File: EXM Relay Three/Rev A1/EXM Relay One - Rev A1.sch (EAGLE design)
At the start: 23 parts, among them J1 MSTBA3, J10 MSTBA2, J2 MSTBA3, J3 22-05-7038-03, J4 22-05-7038-03, J5 22-05-7038-03, J6 22-05-7038-03, J7 MSTBA3, J8 22-05-7038-03, J9 22-05-7038-03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

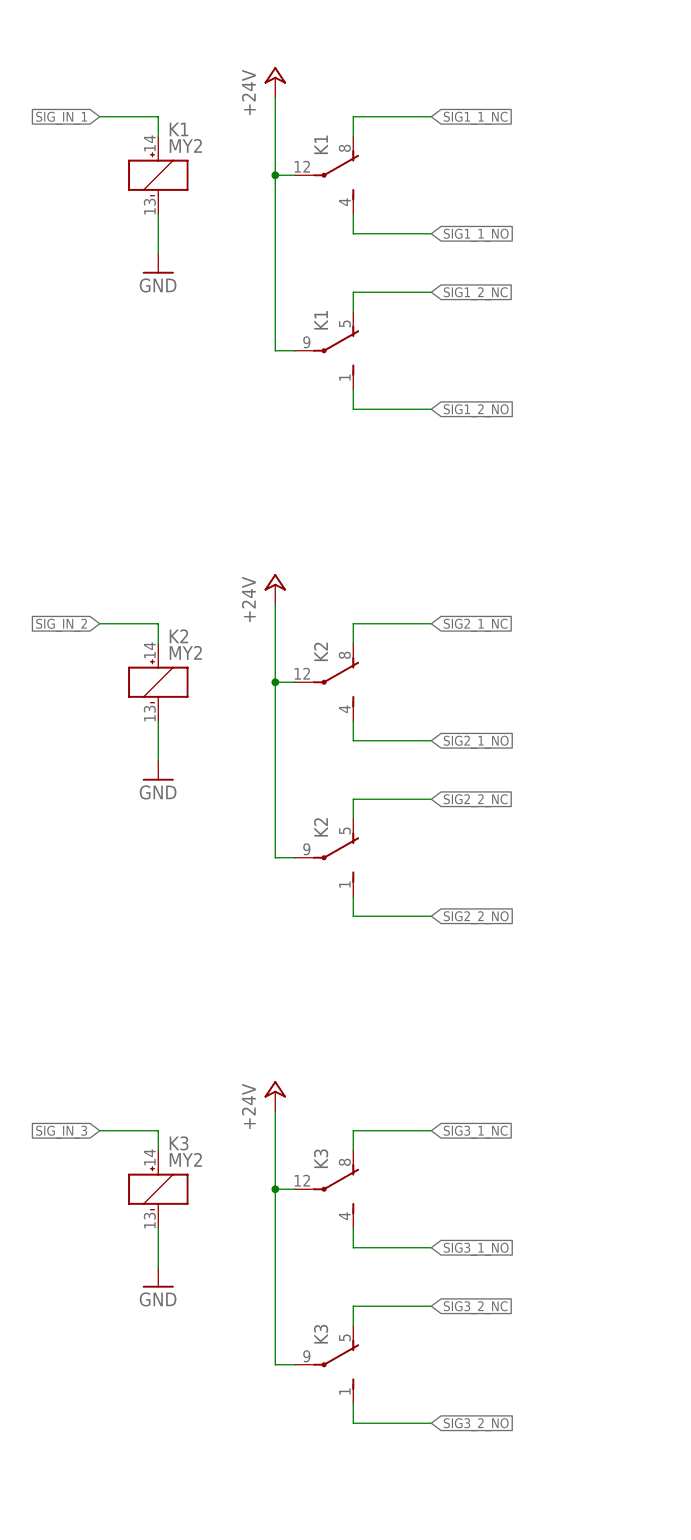
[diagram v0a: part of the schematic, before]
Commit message: Update relay device and re-route the board
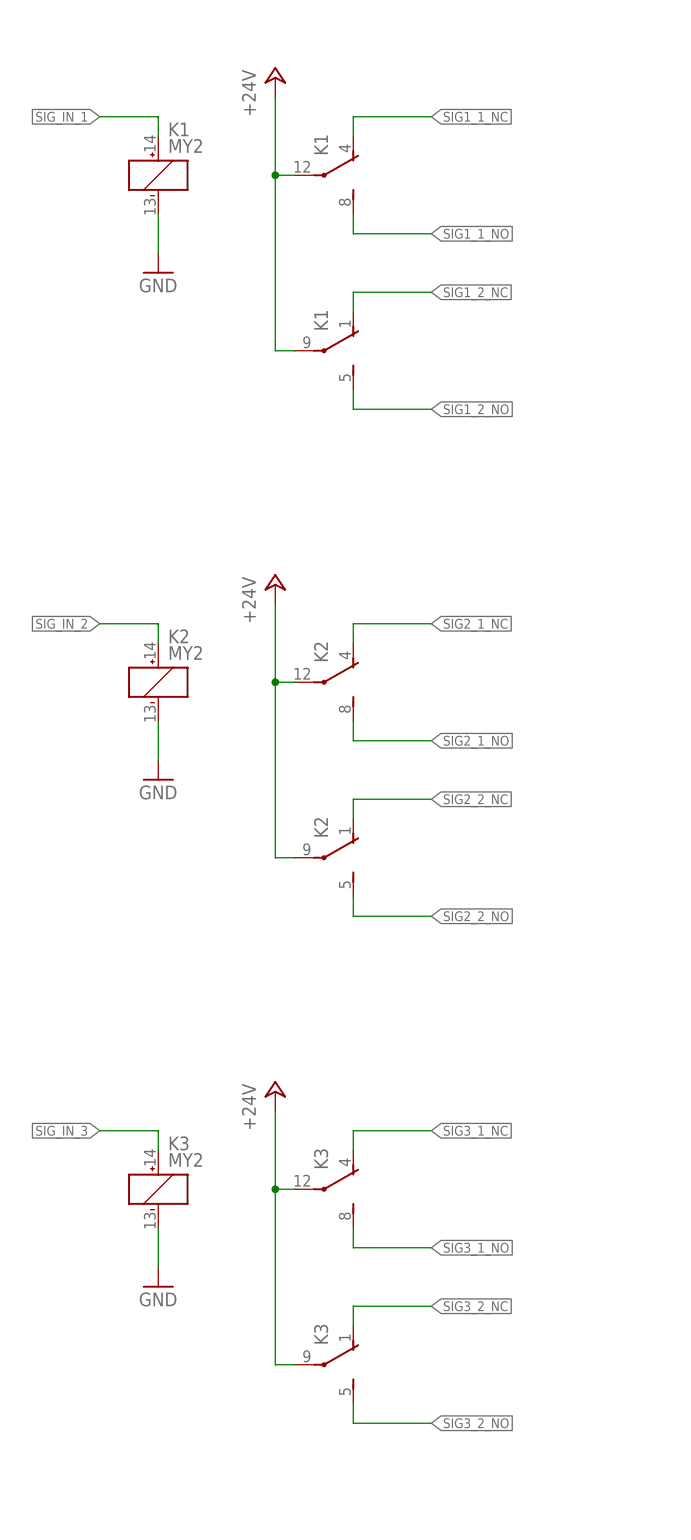
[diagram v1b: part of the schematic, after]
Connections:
- net SIG1_1_NC: now also K1G$2.NC; no longer K1G$2.NO
- net SIG1_1_NO: now also K1G$2.NO; no longer K1G$2.NC
- net SIG1_2_NC: now also K1G$3.NC; no longer K1G$3.NO
- net SIG1_2_NO: now also K1G$3.NO; no longer K1G$3.NC
- net SIG2_1_NC: now also K2G$2.NC; no longer K2G$2.NO
- net SIG2_1_NO: now also K2G$2.NO; no longer K2G$2.NC
- net SIG2_2_NC: now also K2G$3.NC; no longer K2G$3.NO
- net SIG2_2_NO: now also K2G$3.NO; no longer K2G$3.NC
- net SIG3_1_NC: now also K3G$2.NC; no longer K3G$2.NO
- net SIG3_1_NO: now also K3G$2.NO; no longer K3G$2.NC
- net SIG3_2_NC: now also K3G$3.NC; no longer K3G$3.NO
- net SIG3_2_NO: now also K3G$3.NO; no longer K3G$3.NC
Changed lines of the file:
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@@
 <segment>
 <wire x1="167.64" y1="144.78" x2="177.8" y2="144.78" width="0.1524" layer="91"/>
-<pinref part="K2" gate="G$2" pin="NC"/>
-<wire x1="167.64" y1="144.78" x2="167.64" y2="147.32" width="0.1524" layer="91"/>
 <label x="177.8" y="144.78" size="1.27" layer="95" xref="yes"/>
+<pinref part="K2" gate="G$2" pin="NO"/>
+<wire x1="167.64" y1="147.32" x2="167.64" y2="144.78" width="0.1524" layer="91"/>
 </segment>
 </net>
@@
 </segment>
 <segment>
-<pinref part="K1" gate="G$2" pin="NO"/>
-<wire x1="167.64" y1="223.52" x2="167.64" y2="226.06" width="0.1524" layer="91"/>
 <label x="177.8" y="226.06" size="1.27" layer="95" xref="yes"/>
 <wire x1="167.64" y1="226.06" x2="177.8" y2="226.06" width="0.1524" layer="91"/>
+<pinref part="K1" gate="G$2" pin="NC"/>
+<wire x1="167.64" y1="223.52" x2="167.64" y2="226.06" width="0.1524" layer="91"/>
 </segment>
 </net>
 <net name="SIG2_2_NC" class="0">
 <segment>
-<pinref part="K2" gate="G$3" pin="NO"/>
-<wire x1="167.64" y1="134.62" x2="167.64" y2="137.16" width="0.1524" layer="91"/>
 <wire x1="167.64" y1="137.16" x2="177.8" y2="137.16" width="0.1524" layer="91"/>
 <label x="177.8" y="137.16" size="1.27" layer="95" xref="yes"/>
+<pinref part="K2" gate="G$3" pin="NC"/>
+<wire x1="167.64" y1="137.16" x2="167.64" y2="134.62" width="0.1524" layer="91"/>
 </segment>
 <segment>
@@
 <net name="SIG2_2_NO" class="0">
 <segment>
-<pinref part="K2" gate="G$3" pin="NC"/>
-<wire x1="167.64" y1="124.46" x2="167.64" y2="121.92" width="0.1524" layer="91"/>
 <wire x1="167.64" y1="121.92" x2="177.8" y2="121.92" width="0.1524" layer="91"/>
 <label x="177.8" y="121.92" size="1.27" layer="95" xref="yes"/>
+<pinref part="K2" gate="G$3" pin="NO"/>
+<wire x1="167.64" y1="124.46" x2="167.64" y2="121.92" width="0.1524" layer="91"/>
 </segment>
 <segment>
@@
 </segment>
 <segment>
-<pinref part="K2" gate="G$2" pin="NO"/>
-<wire x1="167.64" y1="157.48" x2="167.64" y2="160.02" width="0.1524" layer="91"/>
 <label x="177.8" y="160.02" size="1.27" layer="95" xref="yes"/>
 <wire x1="167.64" y1="160.02" x2="177.8" y2="160.02" width="0.1524" layer="91"/>
+<pinref part="K2" gate="G$2" pin="NC"/>
+<wire x1="167.64" y1="157.48" x2="167.64" y2="160.02" width="0.1524" layer="91"/>
 </segment>
 </net>
@@
 <segment>
 <wire x1="167.64" y1="210.82" x2="177.8" y2="210.82" width="0.1524" layer="91"/>
-<pinref part="K1" gate="G$2" pin="NC"/>
-<wire x1="167.64" y1="210.82" x2="167.64" y2="213.36" width="0.1524" layer="91"/>
 <label x="177.8" y="210.82" size="1.27" layer="95" xref="yes"/>
+<pinref part="K1" gate="G$2" pin="NO"/>
+<wire x1="167.64" y1="213.36" x2="167.64" y2="210.82" width="0.1524" layer="91"/>
 </segment>
 <segment>
@@
 </segment>
 <segment>
-<pinref part="K1" gate="G$3" pin="NC"/>
-<wire x1="167.64" y1="190.5" x2="167.64" y2="187.96" width="0.1524" layer="91"/>
 <wire x1="167.64" y1="187.96" x2="177.8" y2="187.96" width="0.1524" layer="91"/>
 <label x="177.8" y="187.96" size="1.27" layer="95" xref="yes"/>
+<pinref part="K1" gate="G$3" pin="NO"/>
+<wire x1="167.64" y1="190.5" x2="167.64" y2="187.96" width="0.1524" layer="91"/>
 </segment>
 </net>
@@
 </segment>
 <segment>
-<pinref part="K1" gate="G$3" pin="NO"/>
-<wire x1="167.64" y1="200.66" x2="167.64" y2="203.2" width="0.1524" layer="91"/>
 <wire x1="167.64" y1="203.2" x2="177.8" y2="203.2" width="0.1524" layer="91"/>
 <label x="177.8" y="203.2" size="1.27" layer="95" xref="yes"/>
+<pinref part="K1" gate="G$3" pin="NC"/>
+<wire x1="167.64" y1="200.66" x2="167.64" y2="203.2" width="0.1524" layer="91"/>
 </segment>
 </net>
@@
 </segment>
 <segment>
-<pinref part="K3" gate="G$2" pin="NO"/>
-<wire x1="167.64" y1="91.44" x2="167.64" y2="93.98" width="0.1524" layer="91"/>
 <label x="177.8" y="93.98" size="1.27" layer="95" xref="yes"/>
 <wire x1="167.64" y1="93.98" x2="177.8" y2="93.98" width="0.1524" layer="91"/>
+<pinref part="K3" gate="G$2" pin="NC"/>
+<wire x1="167.64" y1="93.98" x2="167.64" y2="91.44" width="0.1524" layer="91"/>
 </segment>
 </net>
@@
 <segment>
 <wire x1="167.64" y1="78.74" x2="177.8" y2="78.74" width="0.1524" layer="91"/>
-<pinref part="K3" gate="G$2" pin="NC"/>
-<wire x1="167.64" y1="78.74" x2="167.64" y2="81.28" width="0.1524" layer="91"/>
 <label x="177.8" y="78.74" size="1.27" layer="95" xref="yes"/>
+<pinref part="K3" gate="G$2" pin="NO"/>
+<wire x1="167.64" y1="81.28" x2="167.64" y2="78.74" width="0.1524" layer="91"/>
 </segment>
 </net>
@@
 </segment>
 <segment>
-<pinref part="K3" gate="G$3" pin="NO"/>
-<wire x1="167.64" y1="68.58" x2="167.64" y2="71.12" width="0.1524" layer="91"/>
 <wire x1="167.64" y1="71.12" x2="177.8" y2="71.12" width="0.1524" layer="91"/>
 <label x="177.8" y="71.12" size="1.27" layer="95" xref="yes"/>
+<pinref part="K3" gate="G$3" pin="NC"/>
+<wire x1="167.64" y1="71.12" x2="167.64" y2="68.58" width="0.1524" layer="91"/>
 </segment>
 </net>
@@
 </segment>
 <segment>
-<pinref part="K3" gate="G$3" pin="NC"/>
-<wire x1="167.64" y1="58.42" x2="167.64" y2="55.88" width="0.1524" layer="91"/>
 <wire x1="167.64" y1="55.88" x2="177.8" y2="55.88" width="0.1524" layer="91"/>
 <label x="177.8" y="55.88" size="1.27" layer="95" xref="yes"/>
+<pinref part="K3" gate="G$3" pin="NO"/>
+<wire x1="167.64" y1="58.42" x2="167.64" y2="55.88" width="0.1524" layer="91"/>
 </segment>
 </net>
